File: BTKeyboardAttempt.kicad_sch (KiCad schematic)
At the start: 14 parts, among them SW1 SW_Push, U2 ATmega32U4-A, Y1 Crystal_GND24_Small

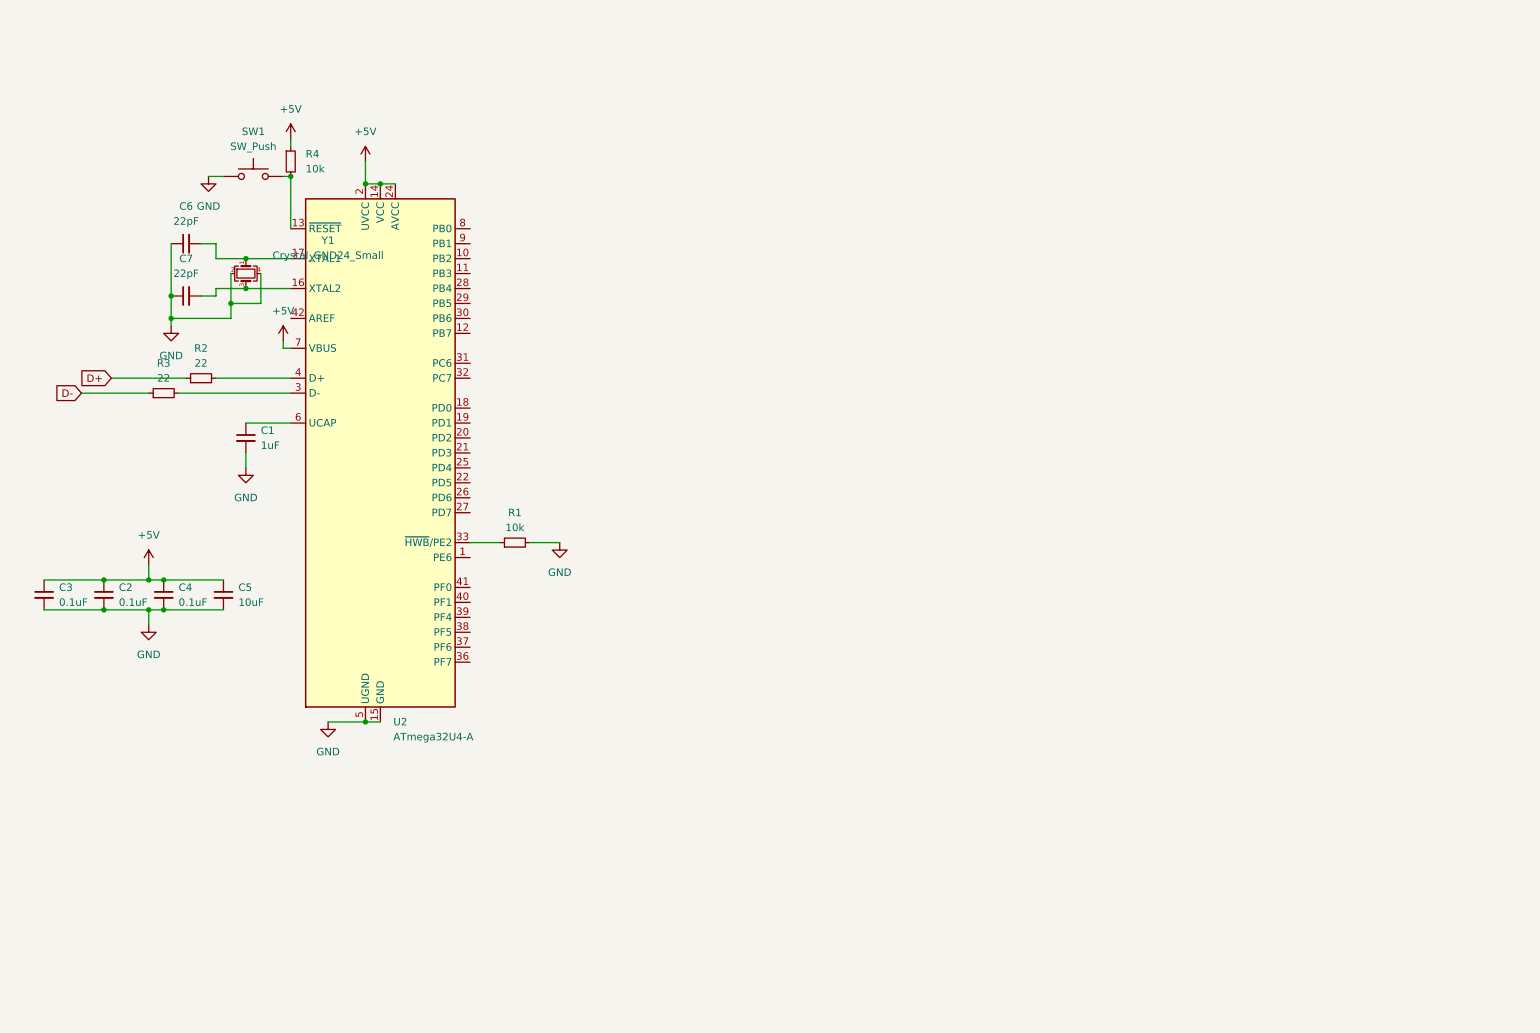
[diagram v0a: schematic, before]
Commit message: schematic complete pcb updated
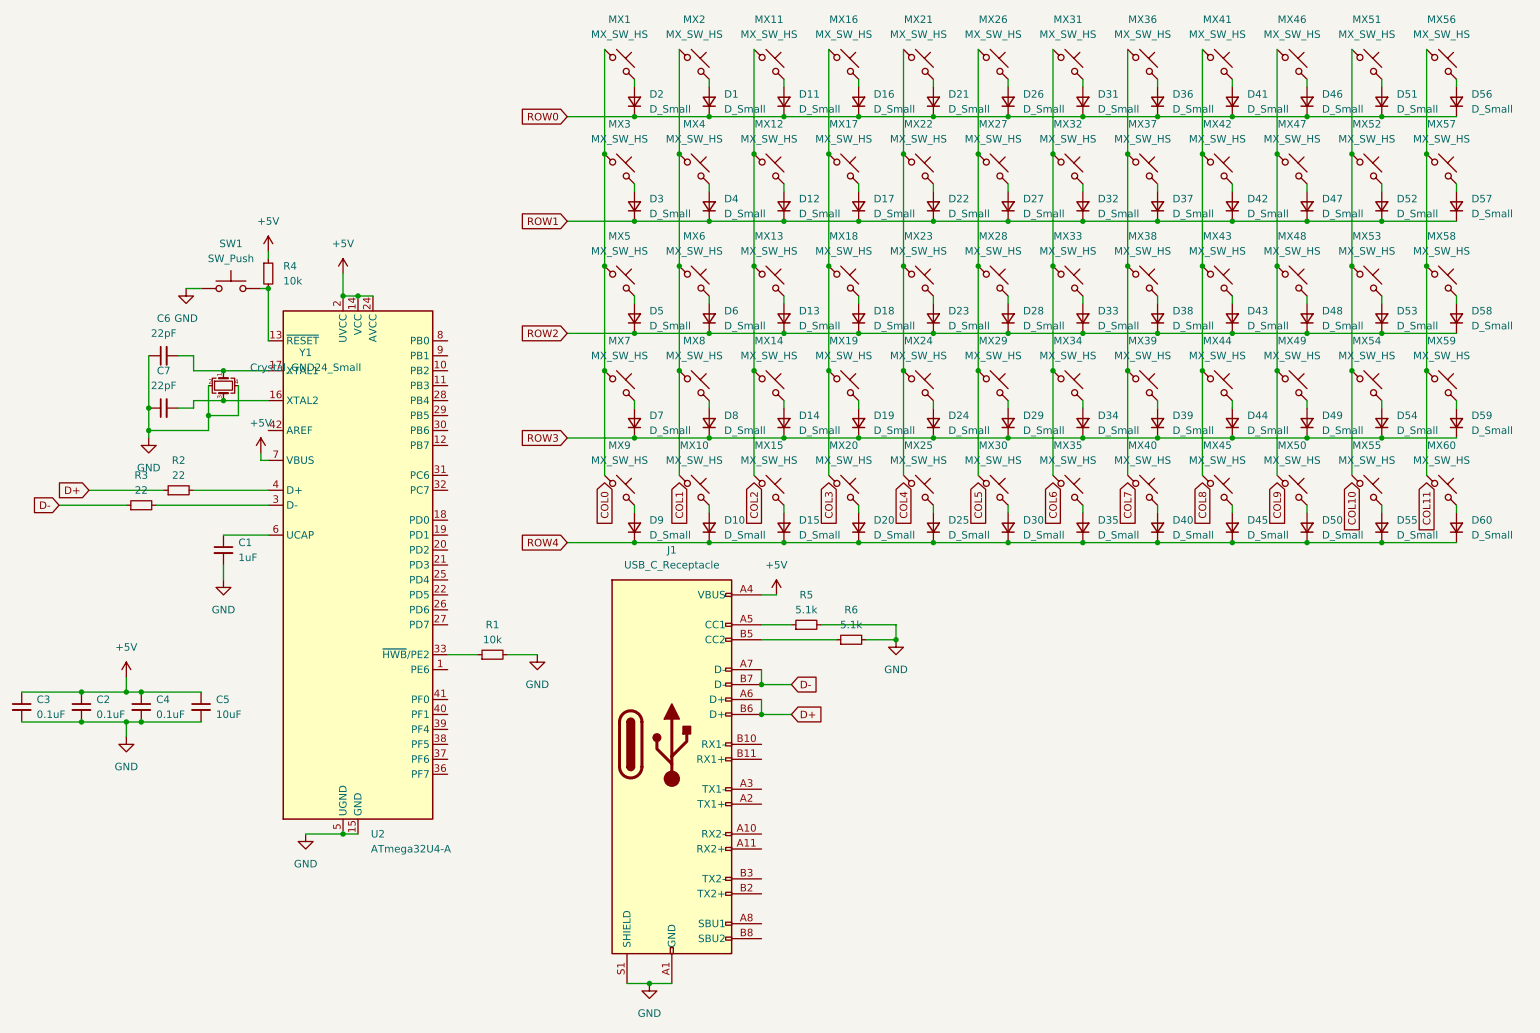
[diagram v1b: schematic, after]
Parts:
- added D1, D10, D11, D12, D13, D14, D15, D16, D17, D18, D19, D2, D20, D21, D22, D23, D24, D25, D26, D27, D28, D29, D3, D30, D31, D32, D33, D34, D35, D36, D37, D38, D39, D4, D40, D41, D42, D43, D44, D45, D46, D47, D48, D49, D5, D50, D51, D52, D53, D54, D55, D56, D57, D58, D59, D6, D60, D7, D8, D9: D_Small, Diode_SMD:D_SOD-123, symbol Device:D_Small
- added J1: USB_C_Receptacle, Connector_USB:USB_C_Receptacle_GCT_USB4125-xx-x_6P_TopMnt_Horizontal, symbol Connector:USB_C_Receptacle
- added MX1, MX10, MX11, MX12, MX13, MX14, MX15, MX16, MX17, MX18, MX19, MX2, MX20, MX21, MX22, MX23, MX24, MX25, MX26, MX27, MX28, MX29, MX3, MX30, MX31, MX32, MX33, MX34, MX35, MX36, MX37, MX38, MX39, MX4, MX40, MX41, MX42, MX43, MX44, MX45, MX46, MX47, MX48, MX49, MX5, MX50, MX51, MX52, MX53, MX54, MX55, MX56, MX57, MX58, MX59, MX6, MX60, MX7, MX8, MX9: MX_SW_HS, PCM_marbastlib-mx:SW_MX_HS_CPG151101S11_1u, symbol PCM_marbastlib-mx:MX_SW_HS_CPG151101S11
- added R5, R6: 5.1k, Resistor_SMD:R_0805_2012Metric, symbol Device:R_Small
- C1, C2, C3, C4, C5, C6, C7: footprint (none) -> Capacitor_SMD:C_0805_2012Metric
- R1, R2, R3, R4: footprint (none) -> Resistor_SMD:R_0805_2012Metric
- SW1: footprint (none) -> Diode_SMD:D_SOD-123
- Y1: footprint (none) -> Crystal:Crystal_SMD_3225-4Pin_3.2x2.5mm
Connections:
- net +5V: now also J1.A4 (VBUS), J1.A9 (VBUS), J1.B4 (VBUS), J1.B9 (VBUS)
- net D+: now also J1.A6 (D+), J1.B6 (D+)
- net D-: now also J1.A7 (D-), J1.B7 (D-)
- net GND: now also J1.A1 (GND), J1.A12 (GND), J1.B1 (GND), J1.B12 (GND), J1.S1 (SHIELD), R5.2, R6.2
- new net: MX10.1, MX2.1, MX4.1, MX6.1, MX8.1
- new net: D4.2 (A), MX4.2
- new net: MX41.1, MX42.1, MX43.1, MX44.1, MX45.1
- new net: D43.2 (A), MX43.2
- new net: MX56.1, MX57.1, MX58.1, MX59.1, MX60.1
- new net: D57.2 (A), MX57.2
- new net: D54.2 (A), MX54.2
- new net: D1.2 (A), MX2.2
- new net: D15.2 (A), MX15.2
- new net: D56.2 (A), MX56.2
- new net: D21.2 (A), MX21.2
- new net: D8.2 (A), MX8.2
- new net: D45.2 (A), MX45.2
- new net: MX21.1, MX22.1, MX23.1, MX24.1, MX25.1
- new net: D22.2 (A), MX22.2
- new net: MX16.1, MX17.1, MX18.1, MX19.1, MX20.1
- new net: D20.2 (A), MX20.2
- new net: D19.2 (A), MX19.2
- new net: MX31.1, MX32.1, MX33.1, MX34.1, MX35.1
- new net: D33.2 (A), MX33.2
- new net: D49.2 (A), MX49.2
- new net: D51.2 (A), MX51.2
- new net: D16.2 (A), MX16.2
- new net: MX26.1, MX27.1, MX28.1, MX29.1, MX30.1
- new net: D27.2 (A), MX27.2
- new net: D28.2 (A), MX28.2
- new net: D34.2 (A), MX34.2
- new net: D29.2 (A), MX29.2
- new net: D46.2 (A), MX46.2
- new net: J1.A5 (CC1), R5.1
- new net: D17.2 (A), MX17.2
- new net: MX36.1, MX37.1, MX38.1, MX39.1, MX40.1
- new net: D40.2 (A), MX40.2
- new net: D42.2 (A), MX42.2
- new net: D36.2 (A), MX36.2
- new net: D59.2 (A), MX59.2
- new net: D6.2 (A), MX6.2
- new net: MX11.1, MX12.1, MX13.1, MX14.1, MX15.1
- new net: D13.2 (A), MX13.2
- new net: MX1.1, MX3.1, MX5.1, MX7.1, MX9.1
- new net: D2.2 (A), MX1.2
- new net: D26.2 (A), MX26.2
- new net: D44.2 (A), MX44.2
- new net: D5.2 (A), MX5.2
- new net: D11.2 (A), MX11.2
- new net: D9.2 (A), MX9.2
- new net: D32.2 (A), MX32.2
- new net: D14.2 (A), MX14.2
- new net: D60.2 (A), MX60.2
- new net: D52.2 (A), MX52.2
- new net: D38.2 (A), MX38.2
- new net: D41.2 (A), MX41.2
- new net: D31.2 (A), MX31.2
- new net: MX51.1, MX52.1, MX53.1, MX54.1, MX55.1
- new net: J1.B5 (CC2), R6.1
- new net: D25.2 (A), MX25.2
- new net: MX46.1, MX47.1, MX48.1, MX49.1, MX50.1
- new net: D50.2 (A), MX50.2
- new net: D47.2 (A), MX47.2
- new net: D48.2 (A), MX48.2
- new net: D39.2 (A), MX39.2
- new net: D3.2 (A), MX3.2
- new net: D35.2 (A), MX35.2
- new net: D58.2 (A), MX58.2
- new net: D18.2 (A), MX18.2
- new net: D12.2 (A), MX12.2
- new net: D55.2 (A), MX55.2
- new net: D37.2 (A), MX37.2
- new net: D10.2 (A), MX10.2
- new net: D24.2 (A), MX24.2
- new net: D23.2 (A), MX23.2
- new net: D30.2 (A), MX30.2
- new net: D7.2 (A), MX7.2
- new net: D53.2 (A), MX53.2
- new net ROW0: D1.1 (K), D11.1 (K), D16.1 (K), D2.1 (K), D21.1 (K), D26.1 (K), D31.1 (K), D36.1 (K), D41.1 (K), D46.1 (K), D51.1 (K), D56.1 (K)
- new net ROW1: D12.1 (K), D17.1 (K), D22.1 (K), D27.1 (K), D3.1 (K), D32.1 (K), D37.1 (K), D4.1 (K), D42.1 (K), D47.1 (K), D52.1 (K), D57.1 (K)
- new net ROW2: D13.1 (K), D18.1 (K), D23.1 (K), D28.1 (K), D33.1 (K), D38.1 (K), D43.1 (K), D48.1 (K), D5.1 (K), D53.1 (K), D58.1 (K), D6.1 (K)
- new net ROW3: D14.1 (K), D19.1 (K), D24.1 (K), D29.1 (K), D34.1 (K), D39.1 (K), D44.1 (K), D49.1 (K), D54.1 (K), D59.1 (K), D7.1 (K), D8.1 (K)
- new net ROW4: D10.1 (K), D15.1 (K), D20.1 (K), D25.1 (K), D30.1 (K), D35.1 (K), D40.1 (K), D45.1 (K), D50.1 (K), D55.1 (K), D60.1 (K), D9.1 (K)
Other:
- moved on the sheet: C1, C2, C3, C4, C5, C6, C7, R1, R2, R3, R4, SW1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

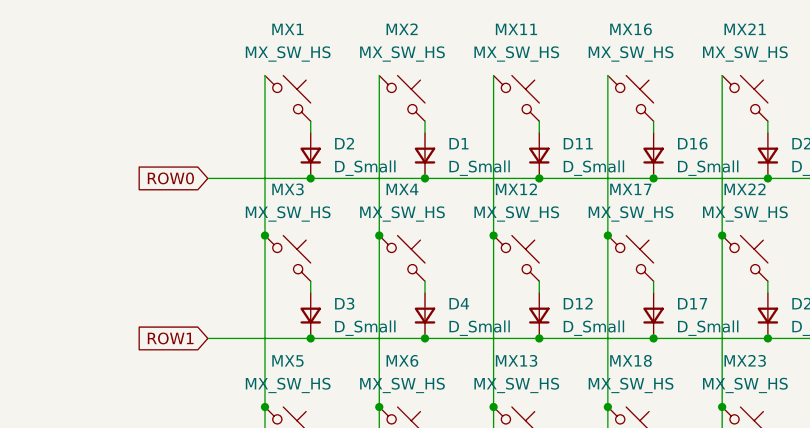
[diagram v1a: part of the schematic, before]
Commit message: Switch and Diode Routing
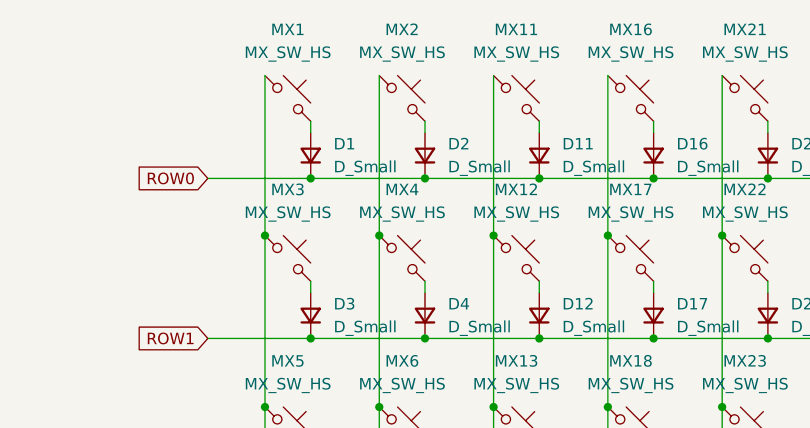
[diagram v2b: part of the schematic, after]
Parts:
- SW1: footprint Diode_SMD:D_SOD-123 -> random-keyboard-parts:SKQG-1155865
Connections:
- net at MX2.2: now also D2.2 (A); no longer D1.2 (A)
- net at MX1.2: now also D1.2 (A); no longer D2.2 (A)
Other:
- moved on the sheet: D1, D2
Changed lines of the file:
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@@
 	)
 	(junction
-		(at 132.08 41.91)
-		(diameter 0)
-		(color 0 0 0 0)
-	)
-	(junction
 		(at 114.3 48.26)
 		(diameter 0)
@@
 	)
 	(junction
+		(at 119.38 41.91)
+		(diameter 0)
+		(color 0 0 0 0)
+	)
+	(junction
 		(at 241.3 48.26)
 		(diameter 0)
@@
 	)
 	(junction
+		(at 132.08 41.91)
+		(diameter 0)
+		(color 0 0 0 0)
+	)
+	(junction
 		(at 152.4 67.31)
 		(diameter 0)
@@
 	)
 	(junction
-		(at 119.38 41.91)
-		(diameter 0)
-		(color 0 0 0 0)
-	)
-	(junction
 		(at 152.4 85.09)
 		(diameter 0)
@@
 	(wire
 		(pts
-			(xy 119.38 41.91) (xy 132.08 41.91)
-		)
-		(stroke
-			(width 0)
-			(type default)
-		)
-	)
-	(wire
-		(pts
 			(xy 203.2 85.09) (xy 203.2 102.87)
 		)
@@
 	(wire
 		(pts
-			(xy 132.08 35.56) (xy 132.08 36.83)
+			(xy 119.38 35.56) (xy 119.38 36.83)
 		)
 		(stroke
@@
 	(wire
 		(pts
+			(xy 119.38 41.91) (xy 132.08 41.91)
+		)
+		(stroke
+			(width 0)
+			(type default)
+		)
+	)
+	(wire
+		(pts
 			(xy 259.08 72.39) (xy 259.08 73.66)
 		)
@@
 	(wire
 		(pts
-			(xy 119.38 35.56) (xy 119.38 36.83)
+			(xy 132.08 35.56) (xy 132.08 36.83)
 		)
 		(stroke
@@
 	(symbol
 		(lib_id "Device:D_Small")
-		(at 119.38 39.37 90)
+		(at 132.08 39.37 90)
 		(unit 1)
 		(exclude_from_sim no)
@@
 		(fields_autoplaced yes)
 		(property "Reference" "D2"
-			(at 121.92 38.0999 90)
+			(at 134.62 38.0999 90)
 			(effects
 				(font
@@
 		)
 		(property "Value" "D_Small"
-			(at 121.92 40.6399 90)
+			(at 134.62 40.6399 90)
 			(effects
 				(font
@@
 		)
 		(property "Footprint" "Diode_SMD:D_SOD-123"
-			(at 119.38 39.37 90)
+			(at 132.08 39.37 90)
 			(effects
 				(font
@@
 		)
 		(property "Datasheet" "~"
-			(at 119.38 39.37 90)
+			(at 132.08 39.37 90)
 			(effects
 				(font
@@
 		)
 		(property "Description" "Diode, small symbol"
-			(at 119.38 39.37 0)
+			(at 132.08 39.37 0)
 			(effects
 				(font
@@
 		)
 		(property "Sim.Device" "D"
-			(at 119.38 39.37 0)
+			(at 132.08 39.37 0)
 			(effects
 				(font
@@
 		)
 		(property "Sim.Pins" "1=K 2=A"
-			(at 119.38 39.37 0)
+			(at 132.08 39.37 0)
 			(effects
 				(font
@@
 	(symbol
 		(lib_id "Device:D_Small")
-		(at 132.08 39.37 90)
+		(at 119.38 39.37 90)
 		(unit 1)
 		(exclude_from_sim no)
@@
 		(fields_autoplaced yes)
 		(property "Reference" "D1"
-			(at 134.62 38.0999 90)
+			(at 121.92 38.0999 90)
 			(effects
 				(font
@@
 		)
 		(property "Value" "D_Small"
-			(at 134.62 40.6399 90)
+			(at 121.92 40.6399 90)
 			(effects
 				(font
@@
 		)
 		(property "Footprint" "Diode_SMD:D_SOD-123"
-			(at 132.08 39.37 90)
+			(at 119.38 39.37 90)
 			(effects
 				(font
@@
 		)
 		(property "Datasheet" "~"
-			(at 132.08 39.37 90)
+			(at 119.38 39.37 90)
 			(effects
 				(font
@@
 		)
 		(property "Description" "Diode, small symbol"
-			(at 132.08 39.37 0)
+			(at 119.38 39.37 0)
 			(effects
 				(font
@@
 		)
 		(property "Sim.Device" "D"
-			(at 132.08 39.37 0)
+			(at 119.38 39.37 0)
 			(effects
 				(font
@@
 		)
 		(property "Sim.Pins" "1=K 2=A"
-			(at 132.08 39.37 0)
+			(at 119.38 39.37 0)
 			(effects
 				(font
@@
 			)
 		)
-		(property "Footprint" "Diode_SMD:D_SOD-123"
+		(property "Footprint" "random-keyboard-parts:SKQG-1155865"
 			(at 50.8 66.04 0)
 			(effects

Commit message: Finished?
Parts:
- J1: footprint Connector_USB:USB_C_Receptacle_GCT_USB4125-xx-x_6P_TopMnt_Horizontal -> Connector_USB:USB_C_Receptacle_Amphenol_12401548E4-2A
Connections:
- net COL0: now also MX1.1, MX3.1, MX5.1, MX7.1, MX9.1, U2.19 (PD1)
- net COL1: now also MX10.1, MX2.1, MX4.1, MX6.1, MX8.1, U2.20 (PD2)
- net COL10: now also MX51.1, MX52.1, MX53.1, MX54.1, MX55.1, U2.31 (PC6)
- net COL11: now also MX56.1, MX57.1, MX58.1, MX59.1, MX60.1, U2.32 (PC7)
- net COL2: now also MX11.1, MX12.1, MX13.1, MX14.1, MX15.1, U2.21 (PD3)
- net COL3: now also MX16.1, MX17.1, MX18.1, MX19.1, MX20.1, U2.22 (PD5)
- net COL4: now also MX21.1, MX22.1, MX23.1, MX24.1, MX25.1, U2.25 (PD4)
- net COL5: now also MX26.1, MX27.1, MX28.1, MX29.1, MX30.1, U2.26 (PD6)
- net COL6: now also MX31.1, MX32.1, MX33.1, MX34.1, MX35.1, U2.27 (PD7)
- net COL7: now also MX36.1, MX37.1, MX38.1, MX39.1, MX40.1, U2.28 (PB4)
- net COL8: now also MX41.1, MX42.1, MX43.1, MX44.1, MX45.1, U2.29 (PB5)
- net COL9: now also MX46.1, MX47.1, MX48.1, MX49.1, MX50.1, U2.30 (PB6)
- net ROW0: now also U2.37 (PF6)
- net ROW1: now also U2.38 (PF5)
- net ROW2: now also U2.39 (PF4)
- net ROW3: now also U2.40 (PF1)
- net ROW4: now also U2.41 (PF0)
